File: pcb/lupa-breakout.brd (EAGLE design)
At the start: 36.5 x 36.1 mm, 19 parts, among them J1 455-1750-1-ND

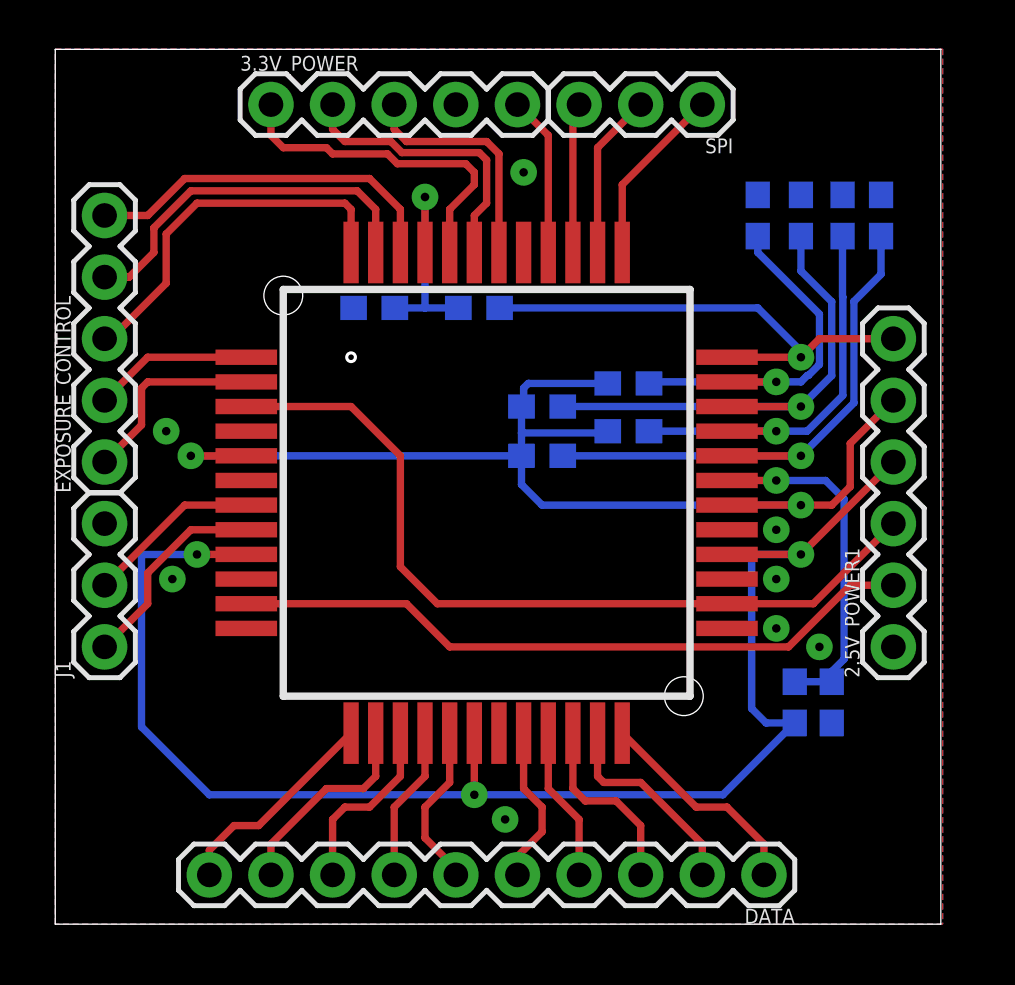
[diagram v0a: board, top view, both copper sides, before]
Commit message: made passices 1206 form factor
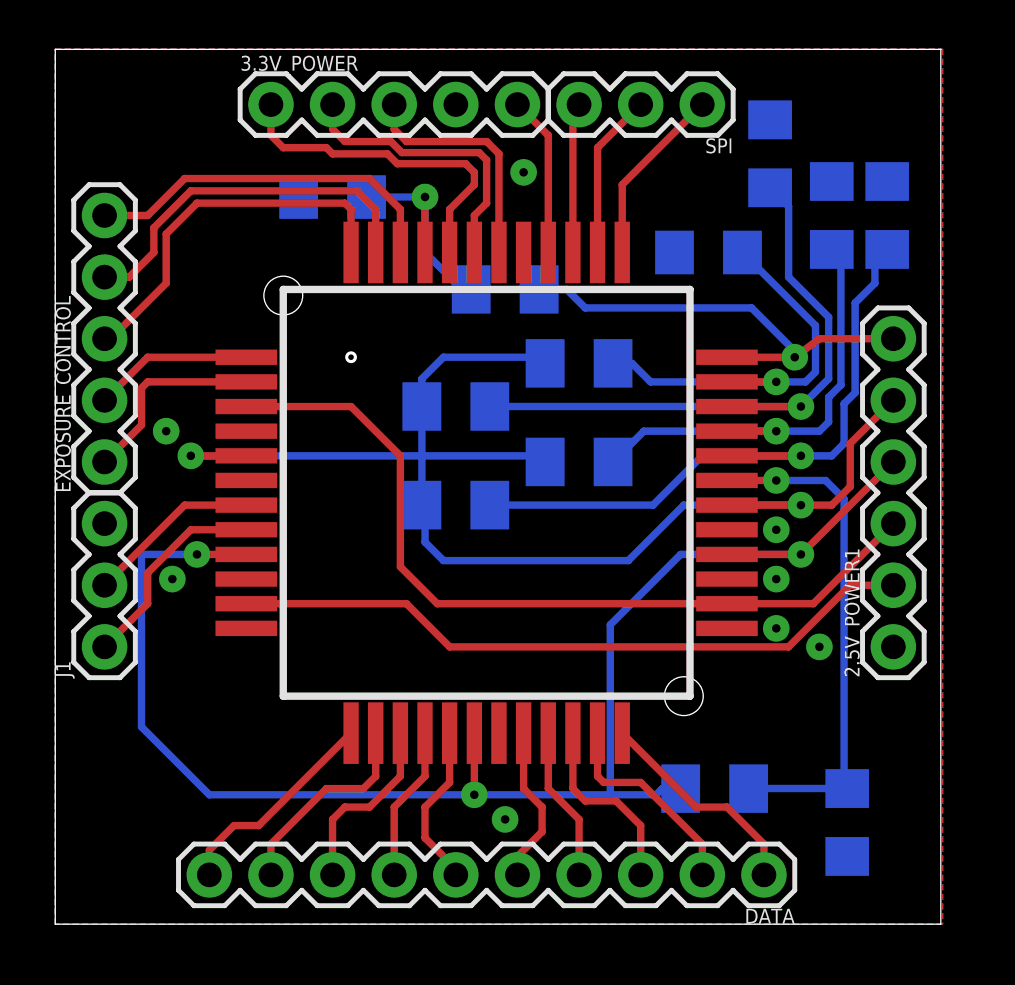
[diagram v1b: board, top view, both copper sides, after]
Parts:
- removed C1, C2, C3, C4, C5, C6: 0.1uF, SparkFun-Capacitors:0603
- removed R1: 10k, SparkFun-Resistors:0603
- removed R2: 110k, SparkFun-Resistors:0603
- removed R3: 1.5M, SparkFun-Resistors:0603
- removed R4: 42k, SparkFun-Resistors:0603
- removed R5: 500k, SparkFun-Resistors:0603
- removed R6: 68k, SparkFun-Resistors:0603
- added C10, C11, C12, C7, C8, C9: 0.1uF, rcl:C1206
- added R10: 42k, resistor:M1206
- added R11: 1.5M, resistor:M1206
- added R12: 500k, resistor:M1206
- added R7: 68k, resistor:M1206
- added R8: 10k, resistor:M1206
- added R9: 110k, resistor:M1206
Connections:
- net ADC_BIAS: now also C8.1, R8.2; no longer C1.1, R1.1
- net BIAS1: now also C12.1, R12.2; no longer C5.1, R5.1
- net BIAS2: now also C11.1, R11.2; no longer C3.1, R3.1
- net BIAS3: now also C10.1, R10.2; no longer C4.1, R4.1
- net BIAS4: now also C9.1, R9.2; no longer C2.1, R2.1
- net GND: now also C10.2, C11.2, C12.2, C7.2, C8.2, C9.2; no longer C1.2, C2.2, C3.2, C4.2, C5.2, C6.2
- net PRECHARGE_BIAS: now also C7.1, R7.2; no longer C6.1, R6.1
- net VADC: now also R8.1; no longer R1.2
- net VDDA: now also R10.1, R11.1, R12.1, R9.1; no longer R2.2, R3.2, R4.2, R5.2
- net VPIX: now also R7.1; no longer R6.2
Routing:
- net VDDA: track 48.6 -> 55.8 mm
- net ADC_BIAS: track 14.4 -> 21.2 mm
- net BIAS2: track 20.9 -> 26.4 mm
- net BIAS4: track 23.3 -> 27.4 mm
- net BIAS3: track 17.2 -> 19.6 mm
- net VPIX: track 20.6 -> 19.0 mm
- net BIAS1: track 15.7 -> 17.0 mm

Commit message: work on lup breakout
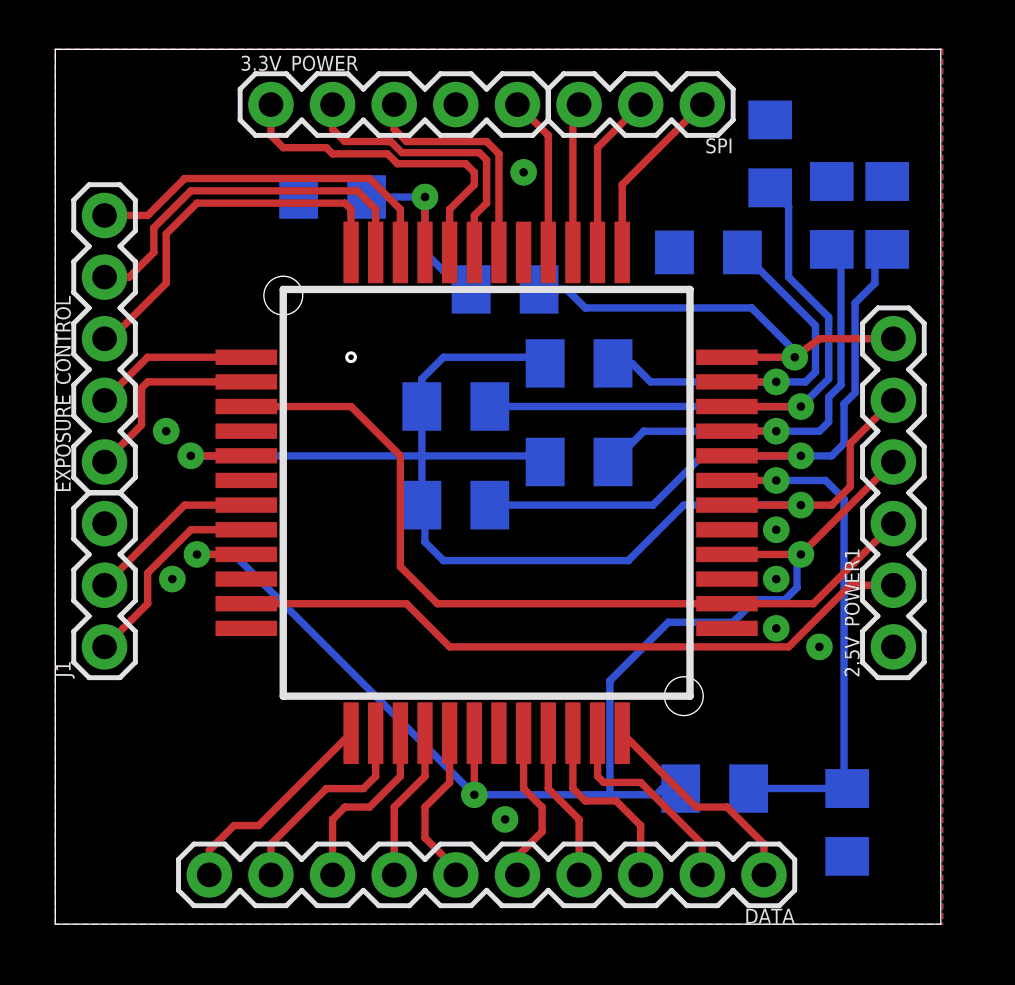
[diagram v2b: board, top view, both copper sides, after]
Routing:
- net VADC: track 62.0 -> 52.6 mm
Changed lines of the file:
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@@
 <via x="17.272" y="5.334" extent="1-16" drill="0.35" diameter="1.1" shape="octagon"/>
 <wire x1="17.272" y1="5.334" x2="17.272" y2="7.874" width="0.3048" layer="1"/>
-<wire x1="5.842" y1="15.24" x2="3.556" y2="15.24" width="0.3048" layer="16"/>
-<wire x1="3.556" y1="15.24" x2="3.556" y2="8.128" width="0.3048" layer="16"/>
-<wire x1="3.556" y1="8.128" x2="6.35" y2="5.334" width="0.3048" layer="16"/>
-<wire x1="6.35" y1="5.334" x2="17.272" y2="5.334" width="0.3048" layer="16"/>
 <via x="30.734" y="15.24" extent="1-16" drill="0.35" diameter="1.1" shape="octagon"/>
 <wire x1="30.734" y1="15.24" x2="27.686" y2="15.24" width="0.3048" layer="1"/>
 <wire x1="34.544" y1="19.05" x2="30.734" y2="15.24" width="0.3048" layer="1"/>
 <contactref element="R8" pad="1"/>
-<wire x1="22.87636875" y1="5.334" x2="17.272" y2="5.334" width="0.3048" layer="16"/>
-<wire x1="22.87636875" y1="5.334" x2="24.765" y2="5.334" width="0.3048" layer="16"/>
+<wire x1="24.765" y1="5.334" x2="22.86" y2="5.334" width="0.3048" layer="16"/>
+<wire x1="17.272" y1="5.334" x2="22.86" y2="5.334" width="0.3048" layer="16"/>
 <wire x1="24.765" y1="5.334" x2="25.019" y2="5.588" width="0.3048" layer="16"/>
 <wire x1="25.019" y1="5.588" x2="25.778" y2="5.588" width="0.3048" layer="16"/>
-<wire x1="25.781" y1="15.24" x2="22.87636875" y2="12.33536875" width="0.3048" layer="16"/>
-<wire x1="22.87636875" y1="12.33536875" x2="22.87636875" y2="5.334" width="0.3048" layer="16"/>
-<wire x1="30.734" y1="15.24" x2="25.781" y2="15.24" width="0.3048" layer="16"/>
+<wire x1="22.86" y1="5.334" x2="22.86" y2="10.033" width="0.3048" layer="16"/>
+<wire x1="22.86" y1="10.033" x2="25.273" y2="12.446" width="0.3048" layer="16"/>
+<wire x1="25.273" y1="12.446" x2="27.94" y2="12.446" width="0.3048" layer="16"/>
+<wire x1="30.072075" y1="13.3692" x2="30.5728" y2="13.869925" width="0.3048" layer="16"/>
+<wire x1="27.94" y1="12.446" x2="28.8632" y2="13.3692" width="0.3048" layer="16"/>
+<wire x1="30.5728" y1="15.0788" x2="30.734" y2="15.24" width="0.3048" layer="16"/>
+<wire x1="28.8632" y1="13.3692" x2="30.072075" y2="13.3692" width="0.3048" layer="16"/>
+<wire x1="30.5728" y1="13.869925" x2="30.5728" y2="15.0788" width="0.3048" layer="16"/>
+<wire x1="5.842" y1="15.24" x2="7.366" y2="15.24" width="0.3048" layer="16"/>
+<wire x1="7.366" y1="15.24" x2="17.272" y2="5.334" width="0.3048" layer="16"/>
 </signal>
 <signal name="GND">

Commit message: finalized breakout for lupa module
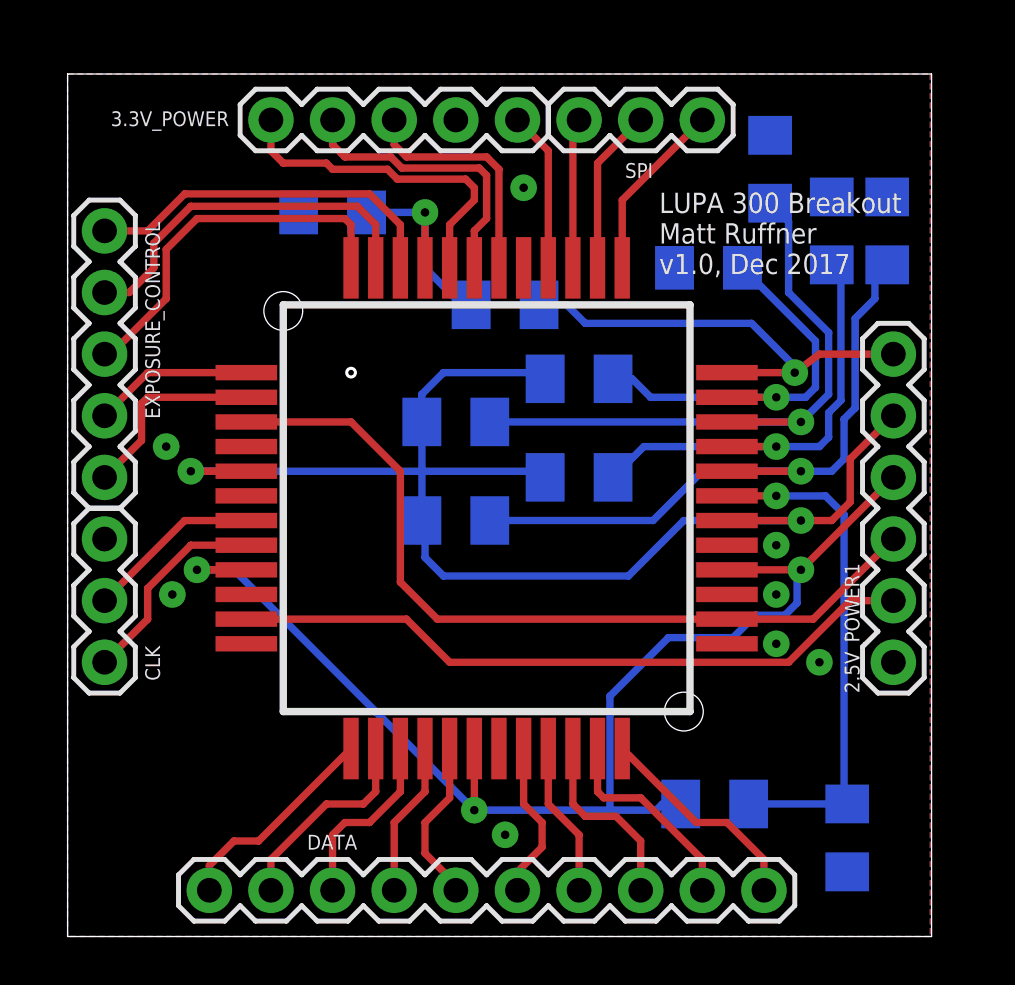
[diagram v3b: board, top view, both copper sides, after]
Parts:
- removed J1: 455-1750-1-ND, SparkFun-Connectors:1X03
- added CLK: 455-1750-1-ND, SparkFun-Connectors:1X03
- C9: value 0.1uF -> .1uF
- moved C10 0.64 mm to (32.0, 28.6)
- moved C11 0.64 mm to (29.5, 31.1)
- moved C12 0.64 mm to (26.9, 27.1)
- moved C7 0.64 mm to (11.4, 29.3)
- moved C9 0.64 mm to (34.3, 28.6)
- moved EXPOSURE_CONTROL 0.64 mm to (2.03, 18.4)
- moved R10 0.64 mm to (21.6, 18.4)
- moved R12 0.64 mm to (21.6, 22.5)
- moved DATA 0.64 mm to (29.2, 1.40)
- moved 2.5V_POWER1 0.63 mm to (34.5, 10.8)
- moved C8 0.63 mm to (32.6, 3.56)
- moved R8 0.63 mm to (27.2, 4.95)
- moved U$1 0.63 mm to (10.7, 10.0)
- moved 3.3V_POWER 0.63 mm to (8.89, 33.1)
- moved R11 0.63 mm to (16.5, 20.7)
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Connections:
- net CLK: now also CLK.1; no longer J1.1
- net GND: now also CLK.3; no longer J1.3
- net RESET: now also CLK.2; no longer J1.2
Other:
- board size 36.5 x 36.1 mm -> 35.6 x 35.6 mm
- board text added: "LUPA 300 Breakout Matt Ruffner v1.0, Dec 2017"

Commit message: made vias smaller and fixed silkscreen
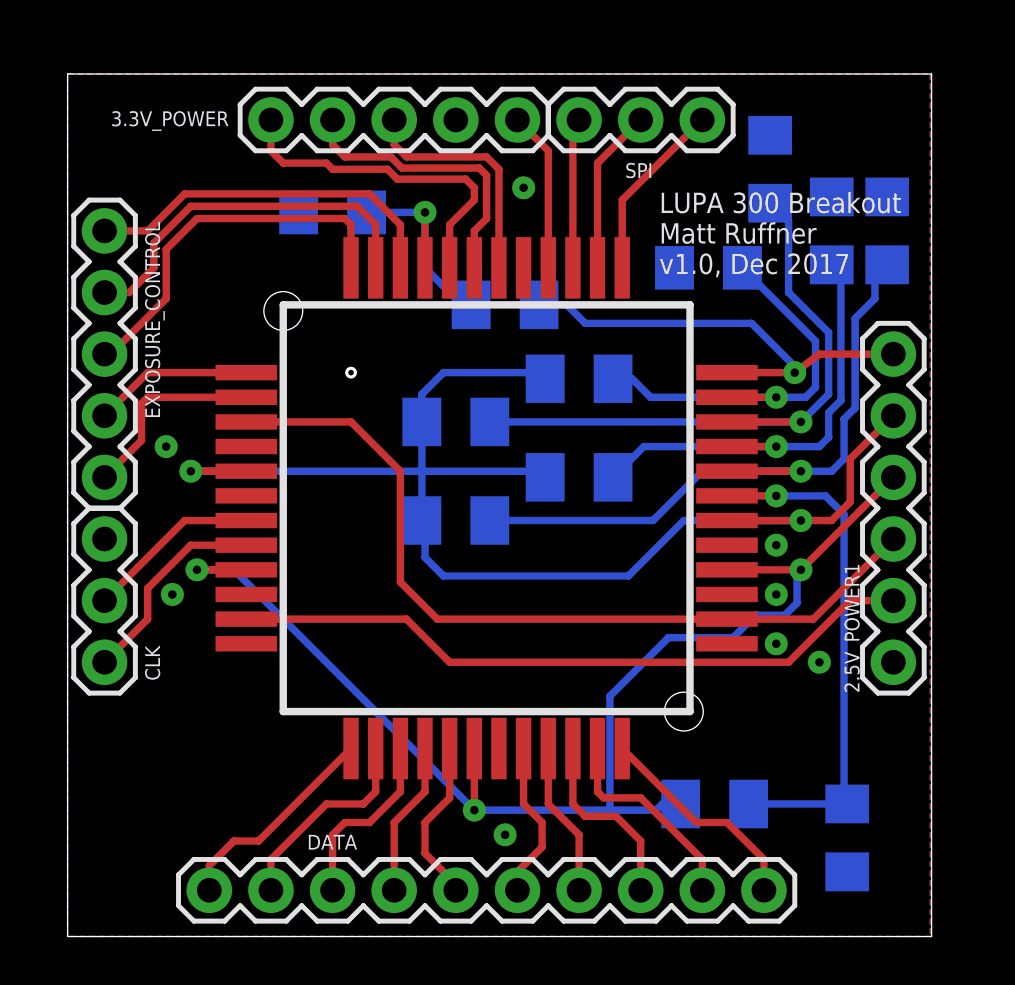
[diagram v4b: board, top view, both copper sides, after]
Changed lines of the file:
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@@
 <contactref element="U$1" pad="P$4"/>
 <contactref element="2.5V_POWER1" pad="4"/>
-<via x="5.842" y="14.605" extent="1-16" drill="0.35" diameter="1.1" shape="octagon"/>
+<via x="5.842" y="14.605" extent="1-16" drill="0.35" diameter="0.95" shape="octagon"/>
 <wire x1="7.874" y1="14.605" x2="5.842" y2="14.605" width="0.3048" layer="1"/>
-<via x="17.272" y="4.699" extent="1-16" drill="0.35" diameter="1.1" shape="octagon"/>
+<via x="17.272" y="4.699" extent="1-16" drill="0.35" diameter="0.95" shape="octagon"/>
 <wire x1="17.272" y1="4.699" x2="17.272" y2="7.239" width="0.3048" layer="1"/>
-<via x="30.734" y="14.605" extent="1-16" drill="0.35" diameter="1.1" shape="octagon"/>
+<via x="30.734" y="14.605" extent="1-16" drill="0.35" diameter="0.95" shape="octagon"/>
 <wire x1="30.734" y1="14.605" x2="27.686" y2="14.605" width="0.3048" layer="1"/>
 <wire x1="34.544" y1="18.415" x2="30.734" y2="14.605" width="0.3048" layer="1"/>
@@
 <contactref element="2.5V_POWER1" pad="1"/>
 <contactref element="CLK" pad="3"/>
-<via x="19.304" y="30.353" extent="1-16" drill="0.35" diameter="1.1" shape="octagon"/>
-<via x="18.542" y="3.683" extent="1-16" drill="0.35" diameter="1.1" shape="octagon"/>
-<via x="4.572" y="19.685" extent="1-16" drill="0.35" diameter="1.1" shape="octagon"/>
-<via x="4.826" y="13.589" extent="1-16" drill="0.35" diameter="1.1" shape="octagon"/>
-<via x="29.718" y="11.557" extent="1-16" drill="0.35" diameter="1.1" shape="octagon"/>
-<via x="29.718" y="15.621" extent="1-16" drill="0.35" diameter="1.1" shape="octagon"/>
-<via x="29.718" y="13.589" extent="1-16" drill="0.35" diameter="1.1" shape="octagon"/>
-<via x="31.496" y="10.795" extent="1-16" drill="0.35" diameter="1.1" shape="octagon"/>
+<via x="19.304" y="30.353" extent="1-16" drill="0.35" diameter="0.95" shape="octagon"/>
+<via x="18.542" y="3.683" extent="1-16" drill="0.35" diameter="0.95" shape="octagon"/>
+<via x="4.572" y="19.685" extent="1-16" drill="0.35" diameter="0.95" shape="octagon"/>
+<via x="4.826" y="13.589" extent="1-16" drill="0.35" diameter="0.95" shape="octagon"/>
+<via x="29.718" y="11.557" extent="1-16" drill="0.35" diameter="0.95" shape="octagon"/>
+<via x="29.718" y="15.621" extent="1-16" drill="0.35" diameter="0.95" shape="octagon"/>
+<via x="29.718" y="13.589" extent="1-16" drill="0.35" diameter="0.95" shape="octagon"/>
+<via x="31.496" y="10.795" extent="1-16" drill="0.35" diameter="0.95" shape="octagon"/>
 <contactref element="C7" pad="2"/>
 <contactref element="C8" pad="2"/>
@@
 <contactref element="U$1" pad="P$19"/>
 <contactref element="2.5V_POWER1" pad="5"/>
-<via x="30.734" y="16.637" extent="1-16" drill="0.35" diameter="1.1" shape="octagon"/>
+<via x="30.734" y="16.637" extent="1-16" drill="0.35" diameter="0.95" shape="octagon"/>
 <wire x1="30.734" y1="16.637" x2="27.686" y2="16.637" width="0.3048" layer="1"/>
 <wire x1="34.544" y1="20.955" x2="32.766" y2="19.177" width="0.3048" layer="1"/>
@@
 <wire x1="32.766" y1="17.399" x2="32.004" y2="16.637" width="0.3048" layer="1"/>
 <wire x1="32.004" y1="16.637" x2="30.734" y2="16.637" width="0.3048" layer="1"/>
-<via x="5.588" y="18.669" extent="1-16" drill="0.35" diameter="1.1" shape="octagon"/>
+<via x="5.588" y="18.669" extent="1-16" drill="0.35" diameter="0.95" shape="octagon"/>
 <wire x1="5.591034375" y1="18.672034375" x2="5.588" y2="18.669" width="0.3048" layer="16"/>
 <wire x1="5.588" y1="18.669" x2="7.874" y2="18.669" width="0.3048" layer="1"/>
@@
 <signal name="ADC_BIAS">
 <contactref element="U$1" pad="P$18"/>
-<via x="29.718" y="17.653" extent="1-16" drill="0.35" diameter="1.1" shape="octagon"/>
+<via x="29.718" y="17.653" extent="1-16" drill="0.35" diameter="0.95" shape="octagon"/>
 <wire x1="27.686" y1="17.653" x2="29.718" y2="17.653" width="0.3048" layer="1"/>
 <wire x1="29.718" y1="17.653" x2="31.75" y2="17.653" width="0.3048" layer="16"/>
@@
 <signal name="BIAS4">
 <contactref element="U$1" pad="P$17"/>
-<via x="30.734" y="18.669" extent="1-16" drill="0.35" diameter="1.1" shape="octagon"/>
+<via x="30.734" y="18.669" extent="1-16" drill="0.35" diameter="0.95" shape="octagon"/>
 <wire x1="27.686" y1="18.669" x2="30.734" y2="18.669" width="0.3048" layer="1"/>
 <contactref element="R9" pad="2"/>
@@
 <signal name="BIAS3">
 <contactref element="U$1" pad="P$16"/>
-<via x="29.718" y="19.685" extent="1-16" drill="0.35" diameter="1.1" shape="octagon"/>
+<via x="29.718" y="19.685" extent="1-16" drill="0.35" diameter="0.95" shape="octagon"/>
 <wire x1="27.686" y1="19.685" x2="29.718" y2="19.685" width="0.3048" layer="1"/>
 <contactref element="R10" pad="2"/>
@@
 <signal name="BIAS2">
 <contactref element="U$1" pad="P$15"/>
-<via x="30.734" y="20.701" extent="1-16" drill="0.35" diameter="1.1" shape="octagon"/>
+<via x="30.734" y="20.701" extent="1-16" drill="0.35" diameter="0.95" shape="octagon"/>
 <wire x1="27.686" y1="20.701" x2="30.734" y2="20.701" width="0.3048" layer="1"/>
 <contactref element="R11" pad="2"/>
@@
 <signal name="BIAS1">
 <contactref element="U$1" pad="P$14"/>
-<via x="29.718" y="21.717" extent="1-16" drill="0.35" diameter="1.1" shape="octagon"/>
+<via x="29.718" y="21.717" extent="1-16" drill="0.35" diameter="0.95" shape="octagon"/>
 <wire x1="27.686" y1="21.717" x2="29.718" y2="21.717" width="0.3048" layer="1"/>
 <wire x1="29.718" y1="21.717" x2="24.5355" y2="21.717" width="0.3048" layer="16"/>
@@
 <contactref element="U$1" pad="P$13"/>
 <contactref element="2.5V_POWER1" pad="6"/>
-<via x="30.48" y="22.733" extent="1-16" drill="0.35" diameter="1.1" shape="octagon"/>
+<via x="30.48" y="22.733" extent="1-16" drill="0.35" diameter="0.95" shape="octagon"/>
 <wire x1="27.686" y1="22.733" x2="30.48" y2="22.733" width="0.3048" layer="1"/>
 <wire x1="30.48" y1="22.733" x2="31.496" y2="23.495" width="0.3048" layer="1"/>
@@
 <signal name="PRECHARGE_BIAS">
 <contactref element="U$1" pad="P$40"/>
-<via x="15.24" y="29.337" extent="1-16" drill="0.35" diameter="1.1" shape="octagon"/>
+<via x="15.24" y="29.337" extent="1-16" drill="0.35" diameter="0.95" shape="octagon"/>
 <wire x1="15.24" y1="29.337" x2="15.24" y2="27.051" width="0.3048" layer="1"/>
 <contactref element="R7" pad="2"/>
